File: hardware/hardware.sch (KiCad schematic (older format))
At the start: 20 parts, among them J1 Conn_01x04_Male, J2 DIN-5_180degree, J3 DIN-5_180degree, SW1 SW_Push, U1 Teensy3.2, U2 TeensyAudioShield3.2, U3 6N139

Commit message: Add extra controls, convert pcb to use connectors
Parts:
- added RV7, RV8: R_POT, Connector_PinHeader_2.54mm:PinHeader_1x03_P2.54mm_Vertical, symbol Device:R_POT
- added SW2: SW_Push, Connector_PinHeader_2.54mm:PinHeader_1x02_P2.54mm_Vertical, symbol Switch:SW_Push
- J2, J3: footprint hardware:SDS-50J -> Connector_PinHeader_2.54mm:PinHeader_1x05_P2.54mm_Vertical
- RV1, RV2, RV3, RV4, RV5, RV6: footprint Potentiometer_THT:Potentiometer_Alpha_RD901F-40-00D_Single_Vertical_CircularHoles -> Connector_PinHeader_2.54mm:PinHeader_1x03_P2.54mm_Vertical
- SW1: footprint Button_Switch_THT:SW_PUSH-12mm -> Connector_PinHeader_2.54mm:PinHeader_1x02_P2.54mm_Vertical
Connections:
- net +3V3: now also RV7.3, RV8.3, SW2.1
- net GND: now also RV7.1, RV8.1
- net LFO1_Amp: now reaches TB1.16 (C7)
- net LFO1_Amp: now also RV7.2
- net LFO1_Freq: now reaches TB1.17 (C8)
- net LFO1_Freq: now also RV8.2
- net LFO1_WAV: now reaches TB1.18 (C9)
- net LFO1_WAV: now also SW2.2
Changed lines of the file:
@@
 F 0 "J3" H 8100 3975 50  0000 C CNN
 F 1 "DIN-5_180degree" H 8100 3884 50  0000 C CNN
-F 2 "hardware:SDS-50J" H 8100 4250 50  0001 C CNN
+F 2 "Connector_PinHeader_2.54mm:PinHeader_1x05_P2.54mm_Vertical" H 8100 4250 50  0001 C CNN
 F 3 "http://www.mouser.com/ds/2/18/40_c091_abd_e-75918.pdf" H 8100 4250 50  0001 C CNN
 	1    8100 4250
@@
 F 0 "J2" H 4025 3975 50  0000 C CNN
 F 1 "DIN-5_180degree" H 4025 3884 50  0000 C CNN
-F 2 "hardware:SDS-50J" H 4025 4250 50  0001 C CNN
+F 2 "Connector_PinHeader_2.54mm:PinHeader_1x05_P2.54mm_Vertical" H 4025 4250 50  0001 C CNN
 F 3 "http://www.mouser.com/ds/2/18/40_c091_abd_e-75918.pdf" H 4025 4250 50  0001 C CNN
 	1    4025 4250
@@
 F 0 "RV1" H 6931 1896 50  0000 R CNN
 F 1 "R_POT" H 6931 1805 50  0000 R CNN
-F 2 "Potentiometer_THT:Potentiometer_Alpha_RD901F-40-00D_Single_Vertical_CircularHoles" H 7000 1850 50  0001 C CNN
+F 2 "Connector_PinHeader_2.54mm:PinHeader_1x03_P2.54mm_Vertical" H 7000 1850 50  0001 C CNN
 F 3 "~" H 7000 1850 50  0001 C CNN
 	1    7000 1850
@@
 F 0 "RV2" H 7531 1896 50  0000 R CNN
 F 1 "R_POT" H 7531 1805 50  0000 R CNN
-F 2 "Potentiometer_THT:Potentiometer_Alpha_RD901F-40-00D_Single_Vertical_CircularHoles" H 7600 1850 50  0001 C CNN
+F 2 "Connector_PinHeader_2.54mm:PinHeader_1x03_P2.54mm_Vertical" H 7600 1850 50  0001 C CNN
 F 3 "~" H 7600 1850 50  0001 C CNN
 	1    7600 1850
@@
 F 0 "RV3" H 8131 1896 50  0000 R CNN
 F 1 "R_POT" H 8131 1805 50  0000 R CNN
-F 2 "Potentiometer_THT:Potentiometer_Alpha_RD901F-40-00D_Single_Vertical_CircularHoles" H 8200 1850 50  0001 C CNN
+F 2 "Connector_PinHeader_2.54mm:PinHeader_1x03_P2.54mm_Vertical" H 8200 1850 50  0001 C CNN
 F 3 "~" H 8200 1850 50  0001 C CNN
 	1    8200 1850
@@
 F 0 "RV4" H 8731 1896 50  0000 R CNN
 F 1 "R_POT" H 8731 1805 50  0000 R CNN
-F 2 "Potentiometer_THT:Potentiometer_Alpha_RD901F-40-00D_Single_Vertical_CircularHoles" H 8800 1850 50  0001 C CNN
+F 2 "Connector_PinHeader_2.54mm:PinHeader_1x03_P2.54mm_Vertical" H 8800 1850 50  0001 C CNN
 F 3 "~" H 8800 1850 50  0001 C CNN
 	1    8800 1850
@@
 F 0 "RV5" H 9331 1896 50  0000 R CNN
 F 1 "R_POT" H 9331 1805 50  0000 R CNN
-F 2 "Potentiometer_THT:Potentiometer_Alpha_RD901F-40-00D_Single_Vertical_CircularHoles" H 9400 1850 50  0001 C CNN
+F 2 "Connector_PinHeader_2.54mm:PinHeader_1x03_P2.54mm_Vertical" H 9400 1850 50  0001 C CNN
 F 3 "~" H 9400 1850 50  0001 C CNN
 	1    9400 1850
@@
 F 0 "RV6" H 9931 1896 50  0000 R CNN
 F 1 "R_POT" H 9931 1805 50  0000 R CNN
-F 2 "Potentiometer_THT:Potentiometer_Alpha_RD901F-40-00D_Single_Vertical_CircularHoles" H 10000 1850 50  0001 C CNN
+F 2 "Connector_PinHeader_2.54mm:PinHeader_1x03_P2.54mm_Vertical" H 10000 1850 50  0001 C CNN
 F 3 "~" H 10000 1850 50  0001 C CNN
 	1    10000 1850
@@
 F 0 "SW1" H 6750 5735 50  0000 C CNN
 F 1 "SW_Push" H 6750 5644 50  0000 C CNN
-F 2 "Button_Switch_THT:SW_PUSH-12mm" H 6750 5650 50  0001 C CNN
+F 2 "Connector_PinHeader_2.54mm:PinHeader_1x02_P2.54mm_Vertical" H 6750 5650 50  0001 C CNN
 F 3 "~" H 6750 5650 50  0001 C CNN
 	1    6750 5450
@@
 Wire Wire Line
 	1550 5850 1700 5850
+$Comp
+L Switch:SW_Push SW2
+U 1 1 5FBF55B0
+P 6750 5825
+F 0 "SW2" H 6750 6110 50  0000 C CNN
+F 1 "SW_Push" H 6750 6019 50  0000 C CNN
+F 2 "Connector_PinHeader_2.54mm:PinHeader_1x02_P2.54mm_Vertical" H 6750 6025 50  0001 C CNN
+F 3 "~" H 6750 6025 50  0001 C CNN
+	1    6750 5825
+	1    0    0    -1
+$EndComp
+$Comp
+L power:+3.3V #PWR0133
+U 1 1 5FBF60CB
+P 6400 5825
+F 0 "#PWR0133" H 6400 5675 50  0001 C CNN
+F 1 "+3.3V" V 6415 5953 50  0000 L CNN
+F 2 "" H 6400 5825 50  0001 C CNN
+F 3 "" H 6400 5825 50  0001 C CNN
+	1    6400 5825
+	0    -1   -1   0
+$EndComp
+Text Label 7100 5825 0    50   ~ 0
+LFO1_WAV
+Wire Wire Line
+	6400 5825 6550 5825
+Wire Wire Line
+	6950 5825 7100 5825
+Text Label 1550 6150 2    50   ~ 0
+LFO1_WAV
+Text Label 1550 5950 2    50   ~ 0
+LFO1_Amp
+Text Label 1550 6050 2    50   ~ 0
+LFO1_Freq
+Wire Wire Line
+	1550 5950 1700 5950
+Wire Wire Line
+	1550 6050 1700 6050
+Wire Wire Line
+	1550 6150 1700 6150
+$Comp
+L Device:R_POT RV7
+U 1 1 5FC14CF2
+P 9425 3075
+F 0 "RV7" H 9356 3121 50  0000 R CNN
+F 1 "R_POT" H 9356 3030 50  0000 R CNN
+F 2 "Connector_PinHeader_2.54mm:PinHeader_1x03_P2.54mm_Vertical" H 9425 3075 50  0001 C CNN
+F 3 "~" H 9425 3075 50  0001 C CNN
+	1    9425 3075
+	1    0    0    -1
+$EndComp
+$Comp
+L Device:R_POT RV8
+U 1 1 5FC14CF8
+P 10025 3075
+F 0 "RV8" H 9956 3121 50  0000 R CNN
+F 1 "R_POT" H 9956 3030 50  0000 R CNN
+F 2 "Connector_PinHeader_2.54mm:PinHeader_1x03_P2.54mm_Vertical" H 10025 3075 50  0001 C CNN
+F 3 "~" H 10025 3075 50  0001 C CNN
+	1    10025 3075
+	1    0    0    -1
+$EndComp
+$Comp
+L power:+3.3V #PWR0134
+U 1 1 5FC14CFE
+P 9425 3375
+F 0 "#PWR0134" H 9425 3225 50  0001 C CNN
+F 1 "+3.3V" H 9440 3548 50  0000 C CNN
+F 2 "" H 9425 3375 50  0001 C CNN
+F 3 "" H 9425 3375 50  0001 C CNN
+	1    9425 3375
+	-1   0    0    1
+$EndComp
+$Comp
+L power:+3.3V #PWR0135
+U 1 1 5FC14D04
+P 10025 3375
+F 0 "#PWR0135" H 10025 3225 50  0001 C CNN
+F 1 "+3.3V" H 10040 3548 50  0000 C CNN
+F 2 "" H 10025 3375 50  0001 C CNN
+F 3 "" H 10025 3375 50  0001 C CNN
+	1    10025 3375
+	-1   0    0    1
+$EndComp
+$Comp
+L power:GND #PWR0136
+U 1 1 5FC14D0A
+P 9425 2725
+F 0 "#PWR0136" H 9425 2475 50  0001 C CNN
+F 1 "GND" H 9430 2552 50  0000 C CNN
+F 2 "" H 9425 2725 50  0001 C CNN
+F 3 "" H 9425 2725 50  0001 C CNN
+	1    9425 2725
+	-1   0    0    1
+$EndComp
+$Comp
+L power:GND #PWR0137
+U 1 1 5FC14D10
+P 10025 2725
+F 0 "#PWR0137" H 10025 2475 50  0001 C CNN
+F 1 "GND" H 10030 2552 50  0000 C CNN
+F 2 "" H 10025 2725 50  0001 C CNN
+F 3 "" H 10025 2725 50  0001 C CNN
+	1    10025 2725
+	-1   0    0    1
+$EndComp
+Text Label 9650 3075 0    50   ~ 0
+LFO1_Amp
+Text Label 10250 3075 0    50   ~ 0
+LFO1_Freq
+Wire Wire Line
+	9575 3075 9650 3075
+Wire Wire Line
+	9425 2725 9425 2925
+Wire Wire Line
+	9425 3375 9425 3225
+Wire Wire Line
+	10025 3375 10025 3225
+Wire Wire Line
+	10025 2925 10025 2725
+Wire Wire Line
+	10250 3075 10175 3075
 $EndSCHEMATC

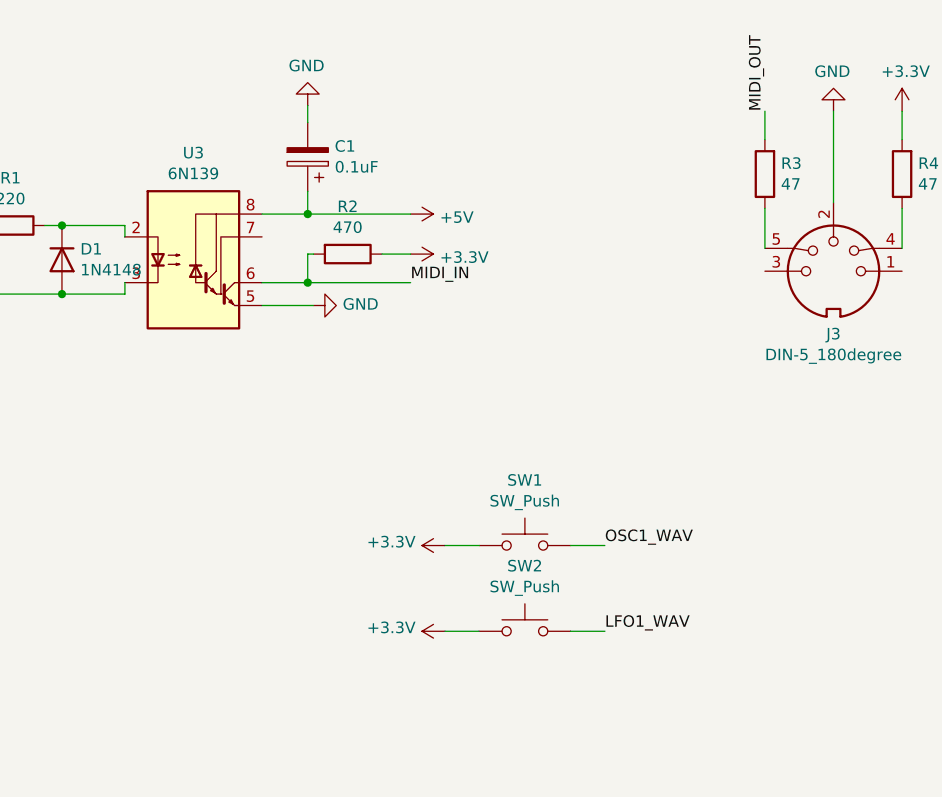
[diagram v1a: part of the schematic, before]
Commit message: Add 6n138 and pull down resistors to schematic
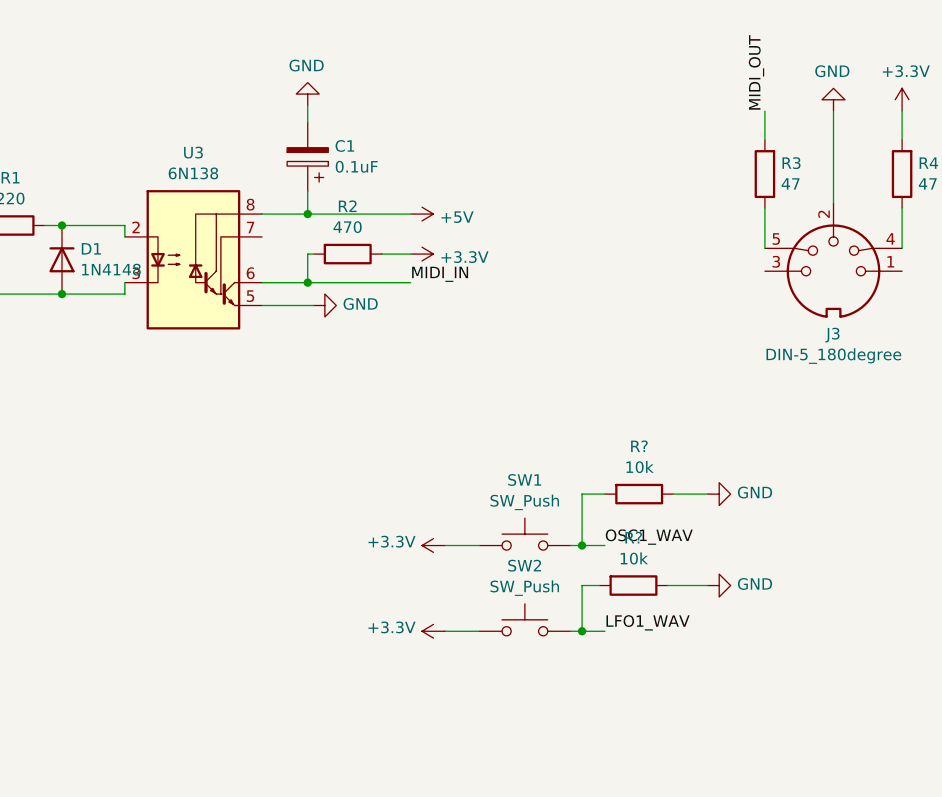
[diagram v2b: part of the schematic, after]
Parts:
- removed U3: 6N139, Package_DIP:DIP-8_W7.62mm_Socket_LongPads, symbol Isolator:6N139
- added R? (x2): 10k, Resistor_THT:R_Axial_DIN0207_L6.3mm_D2.5mm_P10.16mm_Horizontal, symbol Device:R
- added U3: 6N138, symbol Isolator:6N138
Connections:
- net +5V: now also U3.8 (VCC)
- net GND: now also R?.1, R?.1, U3.5 (GND)
- net LFO1_WAV: now also R?.2
- net MIDI_IN: now also U3.6 (VO2)
- net OSC1_WAV: now also R?.2
- net at D1.2 (A), J2.5: now also U3.3 (C2)
- net at D1.1 (K), R1.1: now also U3.2 (C1)
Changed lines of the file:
@@
-$EndComp
-$Comp
-L Isolator:6N139 U3
-U 1 1 5FB479F7
-P 5300 4200
-F 0 "U3" H 5300 4667 50  0000 C CNN
-F 1 "6N139" H 5300 4576 50  0000 C CNN
-F 2 "Package_DIP:DIP-8_W7.62mm_Socket_LongPads" H 5590 3900 50  0001 C CNN
-F 3 "http://www.onsemi.com/pub/Collateral/HCPL2731-D.pdf" H 5590 3900 50  0001 C CNN
-	1    5300 4200
-	1    0    0    -1
 $EndComp
 $Comp
@@
 	6400 5450 6550 5450
 Wire Wire Line
-	6950 5450 7100 5450
+	6950 5450 7000 5450
 $Comp
 L BOB-09056:BOB-09056 TB1
@@
 	6400 5825 6550 5825
 Wire Wire Line
-	6950 5825 7100 5825
+	6950 5825 7000 5825
 Text Label 1550 6150 2    50   ~ 0
 LFO1_WAV
@@
 Wire Wire Line
 	10250 3075 10175 3075
+$Comp
+L Device:R R?
+U 1 1 5FC596A5
+P 7250 5225
+F 0 "R?" V 7043 5225 50  0000 C CNN
+F 1 "10k" V 7134 5225 50  0000 C CNN
+F 2 "Resistor_THT:R_Axial_DIN0207_L6.3mm_D2.5mm_P10.16mm_Horizontal" V 7180 5225 50  0001 C CNN
+F 3 "~" H 7250 5225 50  0001 C CNN
+	1    7250 5225
+	0    1    1    0
+$EndComp
+$Comp
+L Device:R R?
+U 1 1 5FC59B0F
+P 7225 5625
+F 0 "R?" V 7018 5625 50  0000 C CNN
+F 1 "10k" V 7109 5625 50  0000 C CNN
+F 2 "Resistor_THT:R_Axial_DIN0207_L6.3mm_D2.5mm_P10.16mm_Horizontal" V 7155 5625 50  0001 C CNN
+F 3 "~" H 7225 5625 50  0001 C CNN
+	1    7225 5625
+	0    1    1    0
+$EndComp
+$Comp
+L Isolator:6N138 U3
+U 1 1 5FC5ACDD
+P 5300 4200
+F 0 "U3" H 5300 4667 50  0000 C CNN
+F 1 "6N138" H 5300 4576 50  0000 C CNN
+F 2 "" H 5590 3900 50  0001 C CNN
+F 3 "http://www.onsemi.com/pub/Collateral/HCPL2731-D.pdf" H 5590 3900 50  0001 C CNN
+	1    5300 4200
+	1    0    0    -1
+$EndComp
+Wire Wire Line
+	7000 5450 7000 5225
+Wire Wire Line
+	7000 5225 7100 5225
+Connection ~ 7000 5450
+Wire Wire Line
+	7000 5450 7100 5450
+Wire Wire Line
+	7000 5825 7000 5625
+Wire Wire Line
+	7000 5625 7075 5625
+Connection ~ 7000 5825
+Wire Wire Line
+	7000 5825 7100 5825
+$Comp
+L power:GND #PWR?
+U 1 1 5FC7A329
+P 7550 5225
+F 0 "#PWR?" H 7550 4975 50  0001 C CNN
+F 1 "GND" V 7555 5097 50  0000 R CNN
+F 2 "" H 7550 5225 50  0001 C CNN
+F 3 "" H 7550 5225 50  0001 C CNN
+	1    7550 5225
+	0    -1   -1   0
+$EndComp
+$Comp
+L power:GND #PWR?
+U 1 1 5FC7A6DB
+P 7550 5625
+F 0 "#PWR?" H 7550 5375 50  0001 C CNN
+F 1 "GND" V 7555 5497 50  0000 R CNN
+F 2 "" H 7550 5625 50  0001 C CNN
+F 3 "" H 7550 5625 50  0001 C CNN
+	1    7550 5625
+	0    -1   -1   0
+$EndComp
+Wire Wire Line
+	7400 5225 7550 5225
+Wire Wire Line
+	7375 5625 7550 5625
 $EndSCHEMATC

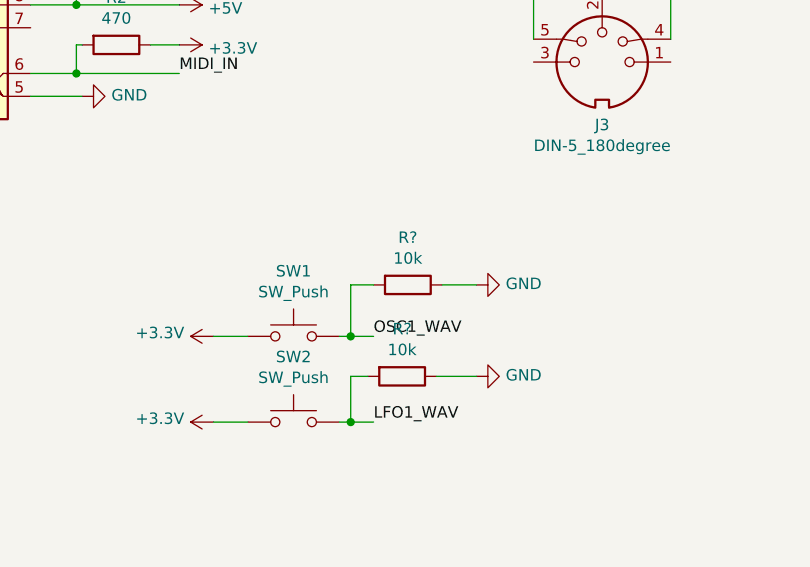
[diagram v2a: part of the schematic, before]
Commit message: Add pull-downs to pcb
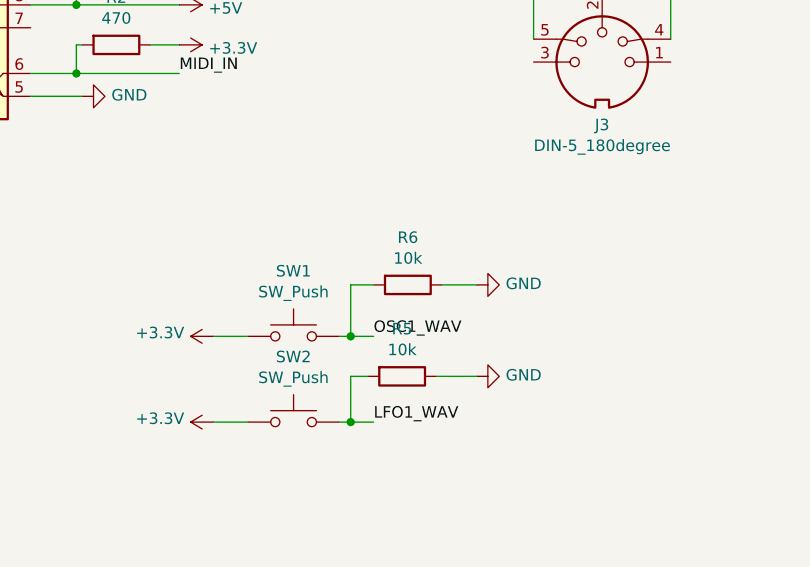
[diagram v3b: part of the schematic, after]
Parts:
- U3: footprint (none) -> Package_DIP:DIP-8_W7.62mm_Socket_LongPads
- gave numbers to parts that had none: 2
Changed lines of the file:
@@
 	10250 3075 10175 3075
 $Comp
-L Device:R R?
+L Device:R R6
 U 1 1 5FC596A5
 P 7250 5225
-F 0 "R?" V 7043 5225 50  0000 C CNN
+F 0 "R6" V 7043 5225 50  0000 C CNN
 F 1 "10k" V 7134 5225 50  0000 C CNN
 F 2 "Resistor_THT:R_Axial_DIN0207_L6.3mm_D2.5mm_P10.16mm_Horizontal" V 7180 5225 50  0001 C CNN
@@
 $EndComp
 $Comp
-L Device:R R?
+L Device:R R5
 U 1 1 5FC59B0F
 P 7225 5625
-F 0 "R?" V 7018 5625 50  0000 C CNN
+F 0 "R5" V 7018 5625 50  0000 C CNN
 F 1 "10k" V 7109 5625 50  0000 C CNN
 F 2 "Resistor_THT:R_Axial_DIN0207_L6.3mm_D2.5mm_P10.16mm_Horizontal" V 7155 5625 50  0001 C CNN
@@
 F 0 "U3" H 5300 4667 50  0000 C CNN
 F 1 "6N138" H 5300 4576 50  0000 C CNN
-F 2 "" H 5590 3900 50  0001 C CNN
+F 2 "Package_DIP:DIP-8_W7.62mm_Socket_LongPads" H 5590 3900 50  0001 C CNN
 F 3 "http://www.onsemi.com/pub/Collateral/HCPL2731-D.pdf" H 5590 3900 50  0001 C CNN
 	1    5300 4200
@@
 	7000 5825 7100 5825
 $Comp
-L power:GND #PWR?
+L power:GND #PWR0138
 U 1 1 5FC7A329
 P 7550 5225
-F 0 "#PWR?" H 7550 4975 50  0001 C CNN
+F 0 "#PWR0138" H 7550 4975 50  0001 C CNN
 F 1 "GND" V 7555 5097 50  0000 R CNN
 F 2 "" H 7550 5225 50  0001 C CNN
@@
 $EndComp
 $Comp
-L power:GND #PWR?
+L power:GND #PWR0139
 U 1 1 5FC7A6DB
 P 7550 5625
-F 0 "#PWR?" H 7550 5375 50  0001 C CNN
+F 0 "#PWR0139" H 7550 5375 50  0001 C CNN
 F 1 "GND" V 7555 5497 50  0000 R CNN
 F 2 "" H 7550 5625 50  0001 C CNN
